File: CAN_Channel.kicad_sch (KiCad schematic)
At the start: 6 parts, among them U6 TJA1051T-3

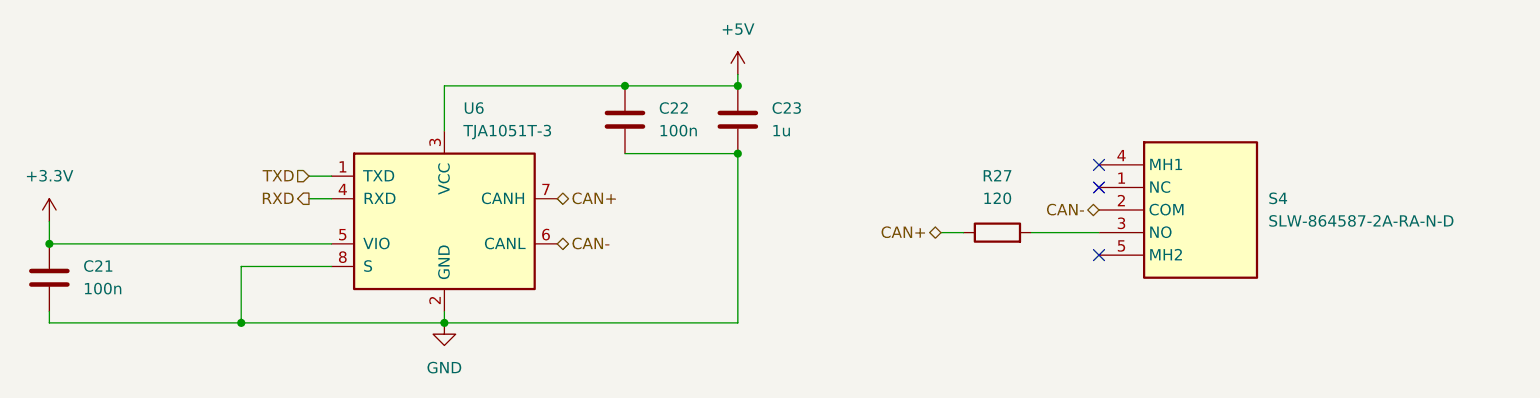
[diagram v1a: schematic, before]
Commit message: finished layout, routing, and silkscreen
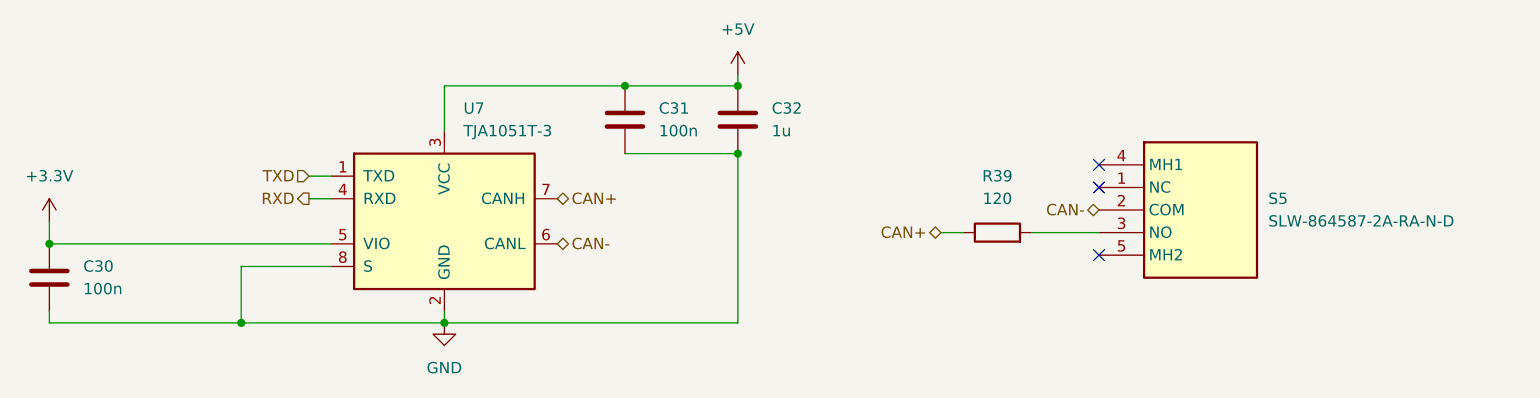
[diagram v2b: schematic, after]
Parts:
- renumbered C21 to C30, C22 to C31, C23 to C32, R27 to R39, S4 to S5, U6 to U7
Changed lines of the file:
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@@
 		(dnp no)
 		(fields_autoplaced yes)
-		(property "Reference" "S4"
+		(property "Reference" "S5"
 			(at 213.36 87.6299 0)
 			(show_name no)
@@
 			(project "RSC-LV3-LVBPS"
 				(path "/4bbf2fff-9f66-421d-84bf-68d1dcd1e11d/7163d647-ae4e-492e-a05d-dd78608c20a5/aa39c3ff-c1bc-401e-97d6-56f59764a03f"
-					(reference "S4")
+					(reference "S5")
 					(unit 1)
 				)
@@
 		(dnp no)
 		(fields_autoplaced yes)
-		(property "Reference" "#PWR050"
+		(property "Reference" "#PWR069"
 			(at 153.67 77.47 0)
 			(hide yes)
@@
 			(project "RSC-LV3-LVBPS"
 				(path "/4bbf2fff-9f66-421d-84bf-68d1dcd1e11d/7163d647-ae4e-492e-a05d-dd78608c20a5/aa39c3ff-c1bc-401e-97d6-56f59764a03f"
-					(reference "#PWR050")
+					(reference "#PWR069")
 					(unit 1)
 				)
@@
 		(dnp no)
 		(fields_autoplaced yes)
-		(property "Reference" "#PWR048"
+		(property "Reference" "#PWR067"
 			(at 76.2 93.98 0)
 			(hide yes)
@@
 			(project "RSC-LV3-LVBPS"
 				(path "/4bbf2fff-9f66-421d-84bf-68d1dcd1e11d/7163d647-ae4e-492e-a05d-dd78608c20a5/aa39c3ff-c1bc-401e-97d6-56f59764a03f"
-					(reference "#PWR048")
+					(reference "#PWR067")
 					(unit 1)
 				)
@@
 		(dnp no)
 		(fields_autoplaced yes)
-		(property "Reference" "#PWR049"
+		(property "Reference" "#PWR068"
 			(at 120.65 107.95 0)
 			(hide yes)
@@
 			(project "RSC-LV3-LVBPS"
 				(path "/4bbf2fff-9f66-421d-84bf-68d1dcd1e11d/7163d647-ae4e-492e-a05d-dd78608c20a5/aa39c3ff-c1bc-401e-97d6-56f59764a03f"
-					(reference "#PWR049")
+					(reference "#PWR068")
 					(unit 1)
 				)
@@
 		(dnp no)
 		(fields_autoplaced yes)
-		(property "Reference" "C21"
+		(property "Reference" "C30"
 			(at 80.01 95.2499 0)
 			(show_name no)
@@
 			(project "RSC-LV3-LVBPS"
 				(path "/4bbf2fff-9f66-421d-84bf-68d1dcd1e11d/7163d647-ae4e-492e-a05d-dd78608c20a5/aa39c3ff-c1bc-401e-97d6-56f59764a03f"
-					(reference "C21")
+					(reference "C30")
 					(unit 1)
 				)
@@
 		(dnp no)
 		(fields_autoplaced yes)
-		(property "Reference" "U6"
+		(property "Reference" "U7"
 			(at 122.7933 77.47 0)
 			(show_name no)
@@
 			(project "RSC-LV3-LVBPS"
 				(path "/4bbf2fff-9f66-421d-84bf-68d1dcd1e11d/7163d647-ae4e-492e-a05d-dd78608c20a5/aa39c3ff-c1bc-401e-97d6-56f59764a03f"
-					(reference "U6")
+					(reference "U7")
 					(unit 1)
 				)
@@
 		(dnp no)
 		(fields_autoplaced yes)
-		(property "Reference" "C22"
+		(property "Reference" "C31"
 			(at 144.78 77.4699 0)
 			(show_name no)
@@
 			(project "RSC-LV3-LVBPS"
 				(path "/4bbf2fff-9f66-421d-84bf-68d1dcd1e11d/7163d647-ae4e-492e-a05d-dd78608c20a5/aa39c3ff-c1bc-401e-97d6-56f59764a03f"
-					(reference "C22")
+					(reference "C31")
 					(unit 1)
 				)
@@
 		(dnp no)
 		(fields_autoplaced yes)
-		(property "Reference" "R27"
+		(property "Reference" "R39"
 			(at 182.88 85.09 90)
 			(show_name no)
@@
 			(project "RSC-LV3-LVBPS"
 				(path "/4bbf2fff-9f66-421d-84bf-68d1dcd1e11d/7163d647-ae4e-492e-a05d-dd78608c20a5/aa39c3ff-c1bc-401e-97d6-56f59764a03f"
-					(reference "R27")
+					(reference "R39")
 					(unit 1)
 				)
@@
 		(dnp no)
 		(fields_autoplaced yes)
-		(property "Reference" "C23"
+		(property "Reference" "C32"
 			(at 157.48 77.4699 0)
 			(show_name no)
@@
 			(project "RSC-LV3-LVBPS"
 				(path "/4bbf2fff-9f66-421d-84bf-68d1dcd1e11d/7163d647-ae4e-492e-a05d-dd78608c20a5/aa39c3ff-c1bc-401e-97d6-56f59764a03f"
-					(reference "C23")
-					(unit 1)
-				)
+					(reference "C32")
+					(unit 1)
+				)
